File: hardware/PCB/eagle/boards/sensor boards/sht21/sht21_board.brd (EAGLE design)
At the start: 14.9 x 12.7 mm, 4 parts

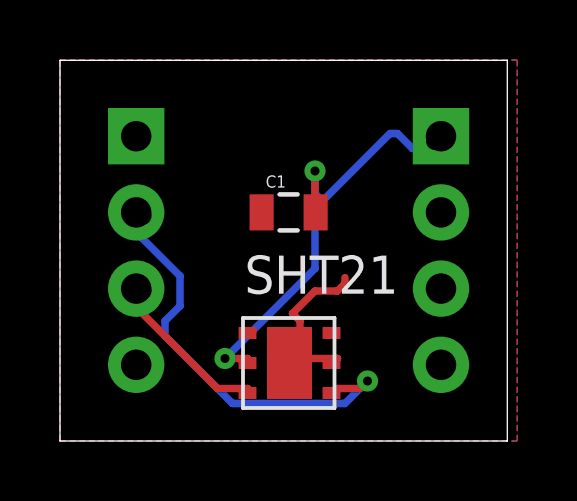
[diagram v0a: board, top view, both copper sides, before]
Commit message: added complete board
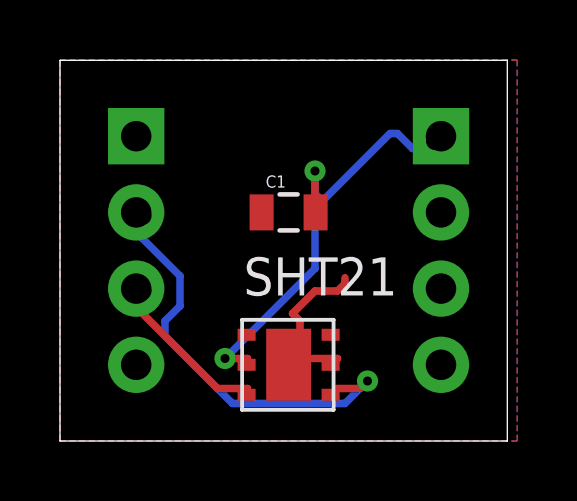
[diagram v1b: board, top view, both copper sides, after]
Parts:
- U$1: value SHT21SHT21 -> SHT21!; device sensors:SHT21 -> integrated_circuits:SHT21
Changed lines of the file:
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@@
 <element name="JP1" library="SparkFun-Connectors" package="1X04" value="" x="2.54" y="6.35" rot="MR270"/>
 <element name="JP2" library="SparkFun-Connectors" package="1X04" value="" x="12.7" y="6.35" rot="MR270"/>
-<element name="U$1" library="sensors" package="SHT21" value="SHT21SHT21" x="7.62" y="2.54"/>
+<element name="U$1" library="integrated_circuits" package="SHT21" value="SHT21!" x="7.62" y="2.54"/>
 </elements>
 <signals>
@@
 <wire x1="2.75" y1="6.75" x2="4" y2="5.5" width="0.25" layer="16"/>
 <wire x1="2.75" y1="7.5" x2="2.75" y2="6.75" width="0.25" layer="16"/>
-<wire x1="9.25" y1="1.75" x2="9.05" y2="1.6" width="0.25" layer="1"/>
+<wire x1="9.25" y1="1.75" x2="9.02" y2="1.54" width="0.25" layer="1"/>
 <wire x1="2.75" y1="7.5" x2="2.54" y2="7.62" width="0.25" layer="1"/>
 <via x="10.25" y="2" extent="1-16" drill="0.3"/>
@@
 <wire x1="2.75" y1="4.25" x2="5.25" y2="1.75" width="0.25" layer="1"/>
 <wire x1="2.75" y1="5" x2="2.75" y2="4.25" width="0.25" layer="1"/>
-<wire x1="6.25" y1="1.75" x2="6.25" y2="1.6" width="0.25" layer="1"/>
+<wire x1="6.25" y1="1.75" x2="6.22" y2="1.54" width="0.25" layer="1"/>
 <wire x1="2.75" y1="5" x2="2.54" y2="5.08" width="0.25" layer="16"/>
 <via x="2.75" y="5" extent="1-16" drill="0.6" shape="square"/>
@@
 <wire x1="12.25" y1="9.75" x2="11.75" y2="9.75" width="0.25" layer="16"/>
 <wire x1="12.5" y1="10" x2="12.25" y2="9.75" width="0.25" layer="16"/>
-<wire x1="6.25" y1="2.75" x2="6.25" y2="2.6" width="0.25" layer="1"/>
+<wire x1="6.25" y1="2.75" x2="6.22" y2="2.54" width="0.25" layer="1"/>
 <wire x1="12.5" y1="10" x2="12.7" y2="10.16" width="0.25" layer="1"/>
 <wire x1="8.5" y1="9" x2="8.5" y2="7.75" width="0.25" layer="1"/>
@@
 </polygon>
 <wire x1="8" y1="2.75" x2="9.25" y2="2.75" width="0.25" layer="1"/>
-<wire x1="9.25" y1="2.75" x2="9.05" y2="2.6" width="0.25" layer="1"/>
-<wire x1="8" y1="2.75" x2="7.65" y2="2.6" width="0.25" layer="1"/>
+<wire x1="9.25" y1="2.75" x2="9.02" y2="2.54" width="0.25" layer="1"/>
+<wire x1="8" y1="2.75" x2="7.62" y2="2.54" width="0.25" layer="1"/>
 <wire x1="8" y1="4" x2="8" y2="3" width="0.25" layer="1"/>
 <wire x1="7.75" y1="4.25" x2="8" y2="4" width="0.25" layer="1"/>
@@
 <wire x1="9.25" y1="5" x2="8.5" y2="5" width="0.25" layer="1"/>
 <wire x1="9.5" y1="5.25" x2="9.25" y2="5" width="0.25" layer="1"/>
-<wire x1="8" y1="3" x2="7.65" y2="2.6" width="0.25" layer="1"/>
+<wire x1="8" y1="3" x2="7.62" y2="2.54" width="0.25" layer="1"/>
 <wire x1="9.5" y1="5.25" x2="9.5" y2="5.443196875" width="0.25" layer="1"/>
 </signal>

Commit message: updated boards with new components
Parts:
- JP1, JP2: device SparkFun-Connectors:1X04 -> passive_components:1X04
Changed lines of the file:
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@@
 <elements>
 <element name="C1" library="passive_components" package="0805-CAP" value="10 uF" x="7.62" y="7.62"/>
-<element name="JP1" library="SparkFun-Connectors" package="1X04" value="" x="2.54" y="6.35" rot="MR270"/>
-<element name="JP2" library="SparkFun-Connectors" package="1X04" value="" x="12.7" y="6.35" rot="MR270"/>
+<element name="JP1" library="passive_components" package="1X04" value="" x="2.54" y="6.35" rot="MR270"/>
+<element name="JP2" library="passive_components" package="1X04" value="" x="12.7" y="6.35" rot="MR270"/>
 <element name="U$1" library="integrated_circuits" package="SHT21" value="SHT21!" x="7.62" y="2.54"/>
 </elements>
